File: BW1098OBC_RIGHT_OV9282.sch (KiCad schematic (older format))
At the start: 32 parts

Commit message: Cleaned up some duplicates, started reorganizing and putting symbols into one luxonis library so the others can be deleted, added SOM Connector footprint
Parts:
- C? (x3): symbol BW1098OBC_IMX378-SchDoc-cache:BW1098OBC_IMX378-SchDoc-rescue_GRM155R71A104JA01D- -> BW1098OBC_TopLevel-rescue:BW1098OBC_IMX378-SchDoc-rescue_GRM155R71A104JA01D--BW1098OBC_IMX378-SchDoc-cache
- C? (x3): symbol BW1098OBC_IMX378-rescue:GRM188R61A106ME69D--BW1098OBC_IMX378-SchDoc-rescue -> BW1098OBC_TopLevel-rescue:GRM188R61A106ME69D--BW1098OBC_IMX378-SchDoc-rescue-BW1098OBC_IMX378-rescue
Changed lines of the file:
@@
 $EndComp
 $Comp
-L BW1098OBC_IMX378-rescue:GRM188R61A106ME69D--BW1098OBC_IMX378-SchDoc-rescue C?
+L BW1098OBC_TopLevel-rescue:GRM188R61A106ME69D--BW1098OBC_IMX378-SchDoc-rescue-BW1098OBC_IMX378-rescue C?
 U 1 1 5FD52FC2
 P 10200 6800
@@
 $EndComp
 $Comp
-L BW1098OBC_IMX378-rescue:GRM188R61A106ME69D--BW1098OBC_IMX378-SchDoc-rescue C?
+L BW1098OBC_TopLevel-rescue:GRM188R61A106ME69D--BW1098OBC_IMX378-SchDoc-rescue-BW1098OBC_IMX378-rescue C?
 U 1 1 5FD52FC1
 P 8700 6800
@@
 $EndComp
 $Comp
-L BW1098OBC_IMX378-rescue:GRM188R61A106ME69D--BW1098OBC_IMX378-SchDoc-rescue C?
+L BW1098OBC_TopLevel-rescue:GRM188R61A106ME69D--BW1098OBC_IMX378-SchDoc-rescue-BW1098OBC_IMX378-rescue C?
 U 1 1 5FD52FC0
 P 7200 6800
@@
 $EndComp
 $Comp
-L BW1098OBC_IMX378-SchDoc-cache:BW1098OBC_IMX378-SchDoc-rescue_GRM155R71A104JA01D- C?
+L BW1098OBC_TopLevel-rescue:BW1098OBC_IMX378-SchDoc-rescue_GRM155R71A104JA01D--BW1098OBC_IMX378-SchDoc-cache C?
 U 1 1 5FD52FBF
 P 6600 6800
@@
 $EndComp
 $Comp
-L BW1098OBC_IMX378-SchDoc-cache:BW1098OBC_IMX378-SchDoc-rescue_GRM155R71A104JA01D- C?
+L BW1098OBC_TopLevel-rescue:BW1098OBC_IMX378-SchDoc-rescue_GRM155R71A104JA01D--BW1098OBC_IMX378-SchDoc-cache C?
 U 1 1 5FD52FBE
 P 8100 6800
@@
 $EndComp
 $Comp
-L BW1098OBC_IMX378-SchDoc-cache:BW1098OBC_IMX378-SchDoc-rescue_GRM155R71A104JA01D- C?
+L BW1098OBC_TopLevel-rescue:BW1098OBC_IMX378-SchDoc-rescue_GRM155R71A104JA01D--BW1098OBC_IMX378-SchDoc-cache C?
 U 1 1 5FD52FBD
 P 9600 6800

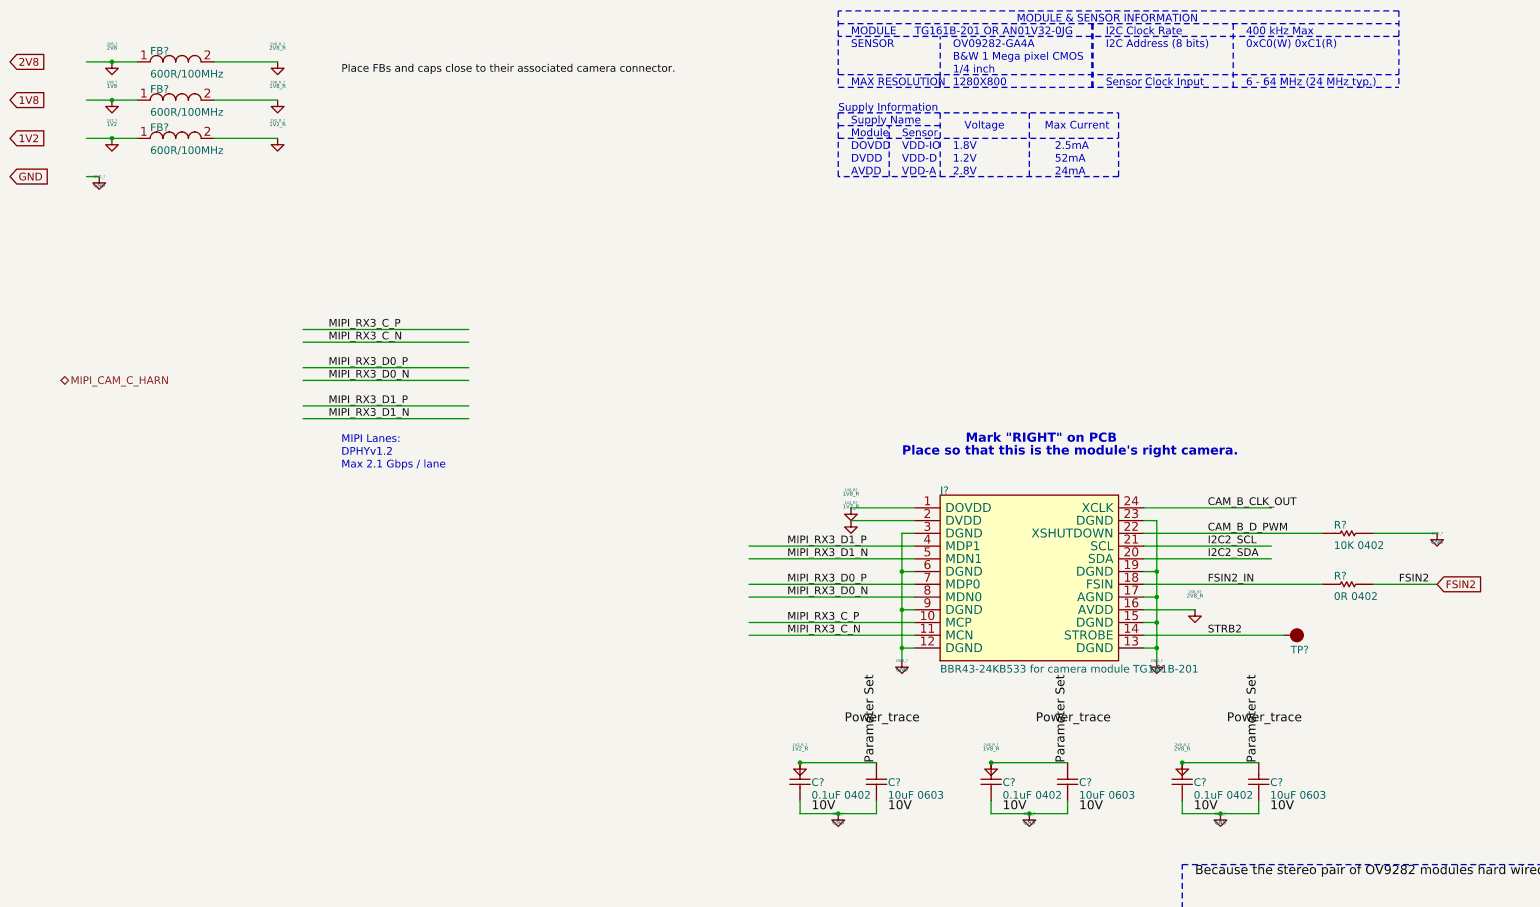
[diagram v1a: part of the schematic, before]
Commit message: More deletion of corrupted or duplicate files, added footprints and associations for mounting holes and 30 pin connector
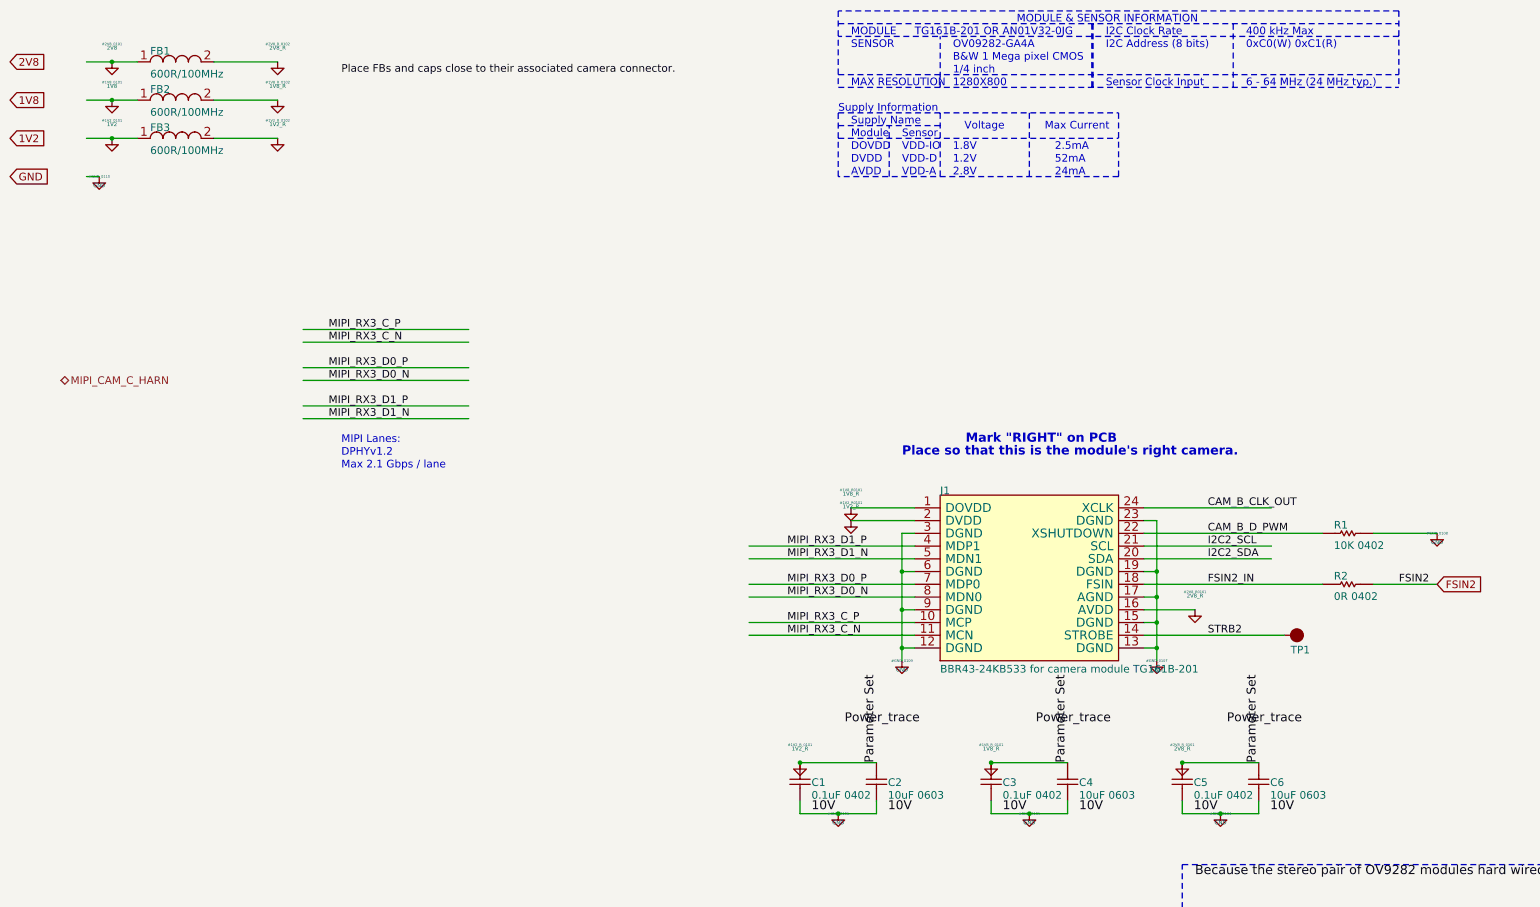
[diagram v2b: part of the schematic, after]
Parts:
- removed 1V2_?: 1V2, symbol power:GND
- removed 1V2_R?, 1V2_R_? (x2): 1V2_R, symbol power:GND
- removed 1V8_?: 1V8, symbol power:GND
- removed 1V8_R?, 1V8_R_? (x2): 1V8_R, symbol power:GND
- removed 2V8_?: 2V8, symbol power:GND
- removed 2V8_R?, 2V8_R_? (x2): 2V8_R, symbol power:GND
- removed GND_? (x7): GND, symbol power:GND
- gave numbers to parts that had none: 13
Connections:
- net labels added: 1V2_R, 1V8_R, 2V8_R
